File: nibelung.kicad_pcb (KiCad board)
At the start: 2 copper layers, 35.6 x 35.6 mm, 47 parts, among them J1 JST_SH_01x03, J2 AudioJack3-TSW, J3 ScrewTerm_01x08_2.54mm, J4 ScrewTerm_01x08_2.54mm, J5 JST_SH_01x03, J6 JST_SH_01x03, U1 74HCT245, U2 LTC2850xS8, U3 Teensy4.0

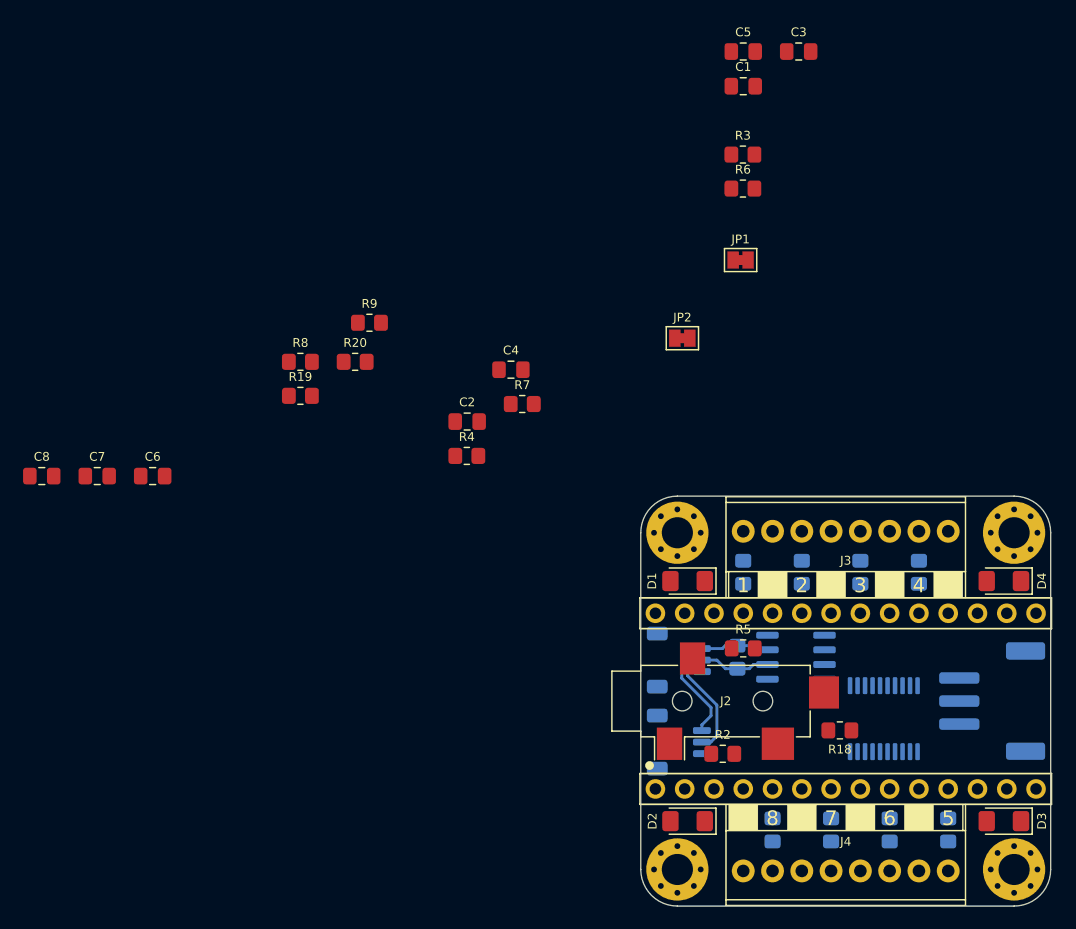
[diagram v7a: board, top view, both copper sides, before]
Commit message: Add linear regulators
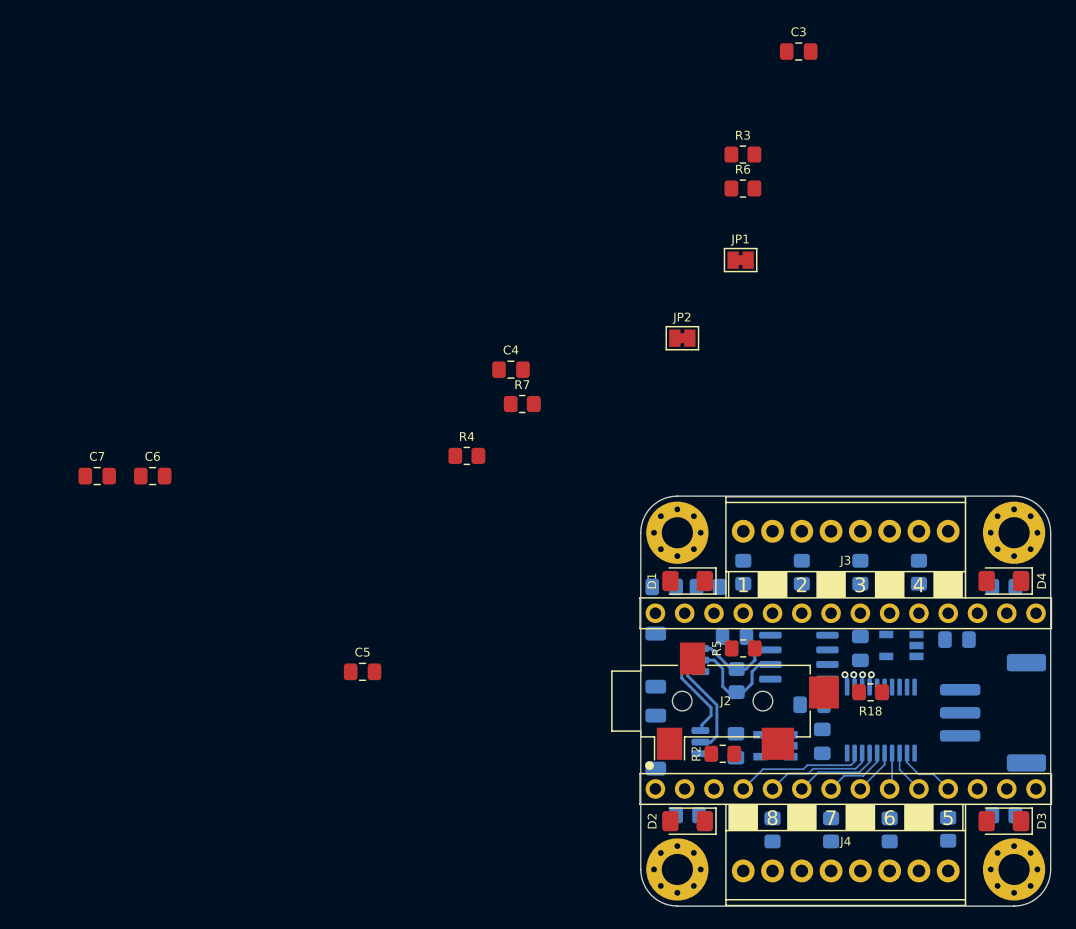
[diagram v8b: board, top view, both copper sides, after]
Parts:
- added C10: 10uF, Capacitor_SMD:C_0805_2012Metric_Pad1.18x1.45mm_HandSolder, B.Cu at (121.9, 97.0)
- added C11: 1uF, Capacitor_SMD:C_0805_2012Metric_Pad1.18x1.45mm_HandSolder, B.Cu at (118.6, 105.1)
- added C12: 1uF, Capacitor_SMD:C_0805_2012Metric_Pad1.18x1.45mm_HandSolder, B.Cu at (111.1, 105.5)
- added C9: 10uF, Capacitor_SMD:C_0805_2012Metric_Pad1.18x1.45mm_HandSolder, B.Cu at (130.3, 96.3)
- added U3: MIC5219-5.0YM5, Package_TO_SOT_SMD:TSOT-23-5, B.Cu at (125.5, 96.8)
- added U4: ADP122AUJZ-3.3, Package_TO_SOT_SMD:TSOT-23-5, B.Cu at (114.6, 105.5)
- C1, C2, C8, R19, R20, R8, R9: moved to B.Cu
- D2: value AMBER -> BLUE
- D3: value GREEN -> YEL
- D4: value BLUE -> GRN
- moved R19 71.0 mm to (134.4, 111.5), turned to 180 degrees
- moved C8 69.7 mm to (117.7, 101.9)
- moved C5 63.1 mm to (78.7, 99.1)
- moved R20 59.6 mm to (134.4, 91.7), turned to 180 degrees
- moved R9 50.9 mm to (106.9, 111.5), turned to 180 degrees
- moved C1 47.8 mm to (111.0, 96.0)
- moved R8 40.4 mm to (108.7, 91.7), turned to 180 degrees
- moved R10 22.5 mm to (114.3, 112.8), turned to 90 degrees
- moved R11 22.5 mm to (119.4, 112.8), turned to 90 degrees
- moved R12 22.5 mm to (124.5, 112.8), turned to 90 degrees
- moved R14 22.5 mm to (127.0, 90.4), turned to 270 degrees
- moved R15 22.5 mm to (121.9, 90.4), turned to 270 degrees
- moved R16 22.5 mm to (116.8, 90.4), turned to 270 degrees
- moved R17 22.5 mm to (111.8, 90.4), turned to 270 degrees
- moved R13 22.4 mm to (129.5, 112.7), turned to 90 degrees
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- renumbered U3 to A1
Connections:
- A1 pad 16: Net-(JP2-Pad1) -> /AUD_L_ADC
- A1 pad 17: Net-(JP1-Pad1) -> /AUD_R_ADC
- A1 pad 26: +3V3 -> Net-(A1-Pad26)
- JP1 pad 2: /AUD_R_ADC -> Net-(JP1-Pad2)
- JP2 pad 2: /AUD_L_ADC -> Net-(JP2-Pad2)
- R10 pad 1: /LED_OUT1 -> /LED_OUT8
- R11 pad 1: /LED_OUT2 -> /LED_OUT7
- R12 pad 1: /LED_OUT3 -> /LED_OUT6
- R13 pad 1: /LED_OUT4 -> /LED_OUT5
- R14 pad 1: /LED_OUT5 -> /LED_OUT4
- R15 pad 1: /LED_OUT6 -> /LED_OUT3
- R16 pad 1: /LED_OUT7 -> /LED_OUT2
- R17 pad 1: /LED_OUT8 -> /LED_OUT1
- U1 pad 2: /LED1 -> /LED8
- U1 pad 3: /LED2 -> /LED7
- U1 pad 4: /LED3 -> /LED6
- U1 pad 5: /LED4 -> /LED5
- U1 pad 6: /LED5 -> /LED4
- U1 pad 7: /LED6 -> /LED3
- U1 pad 8: /LED7 -> /LED2
- U1 pad 9: /LED8 -> /LED1
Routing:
- net /LED1: track 0.00 -> 11.4 mm
- net /LED2: track 0.00 -> 9.40 mm
- net /LED3: track 0.00 -> 7.50 mm
- net /LED4: track 0.00 -> 5.60 mm
- net /LED8: track 0.00 -> 5.21 mm
- net /LED5: track 0.00 -> 3.85 mm
- net /LED7: track 0.00 -> 3.67 mm
- net /A: track 16.4 -> 20.1 mm
- net /LED6: track 0.00 -> 3.43 mm
- net /B: track 15.7 -> 17.5 mm
- net Net-(R16-Pad2): track 0.00 -> 1.19 mm, vias 0 -> 1
- net Net-(R17-Pad2): track 0.00 -> 1.16 mm, vias 0 -> 1
- net Net-(R14-Pad2): track 0.00 -> 1.14 mm, vias 0 -> 1
- net Net-(R15-Pad2): track 0.00 -> 1.09 mm, vias 0 -> 1
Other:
- net class Default: clearance 0.254 -> 0.2032
- rule trace_clearance: 0.254 -> 0.2032
- board text added: "RS485"
